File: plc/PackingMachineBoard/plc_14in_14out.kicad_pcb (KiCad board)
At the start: 2 copper layers, 208.3 x 160 mm, 241 parts, among them J1 Screw_Terminal_01x02, J10 Screw_Terminal_01x06, J11 Screw_Terminal_01x02, J12 Ethernet, J13 Screw_Terminal_01x04, J14 CAN, J15 SERIAL_1, J16 I2C0, J17 I2C1, J18 Screw_Terminal_01x01, J19 SERIAL_5, J2 Screw_Terminal_01x06, J20 Screw_Terminal_01x01, J21 Screw_Terminal_01x01, J22 Screw_Terminal_01x01, J23 Screw_Terminal_01x01, J24 Screw_Terminal_01x01, J25 Screw_Terminal_01x01, J3 Screw_Terminal_01x10, J4 Screw_Terminal_01x05, J5 Screw_Terminal_01x05, J6 RJ45_LED, J7 Screw_Terminal_01x06, J8 Screw_Terminal_01x06, J9 Screw_Terminal_01x06, K1 UMS05-1A80-75L, K2 UMS05-1A80-75L, K3 UMS05-1A80-75L, K4 UMS05-1A80-75L, K5 UMS05-1A80-75L, K6 UMS05-1A80-75L, K7 UMS05-1A80-75L, K8 UMS05-1A80-75L, Q1 IRG4PF50W, Q2 IRG4PF50W, Q3 IRG4PF50W, Q4 IRG4PF50W, Q5 IRG4PF50W, Q6 IRG4PF50W, Q7 IRG4PF50W, SW1 SW_DIP_x01, SW2 SW_DIP_x01, SW3 SW_DIP_x01, SW4 Prog, SW5 SW_DIP_x01, SW6 SW_DIP_x01, U1 tlp127, U10 TLP127, U11 tlp127, U12 tlp127, U13 tlp127, U14 tlp127, U15 74HC14, U16 74HC14, U17 74HC14, U18 74HC245, U19 Teensy3.5_All_Pins, U2 tlp127, U20 74HC245, U21 ULN2803A, U22 74AHCT125, U23 74AHCT125, U24 ENC28J60x-SS, U25 LD1117S33TR_SOT223, U26 74AHCT125, U27 74AHCT125, U28 TLP127, U29 TLP127, U3 tlp127, U30 TLP127, U31 TLP127, U32 TLP127, U33 TLP127, U34 tlp127, U35 TLP127, U36 LM7810_TO220, U4 tlp127, U5 tlp127, U6 tlp127, U7 tlp127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

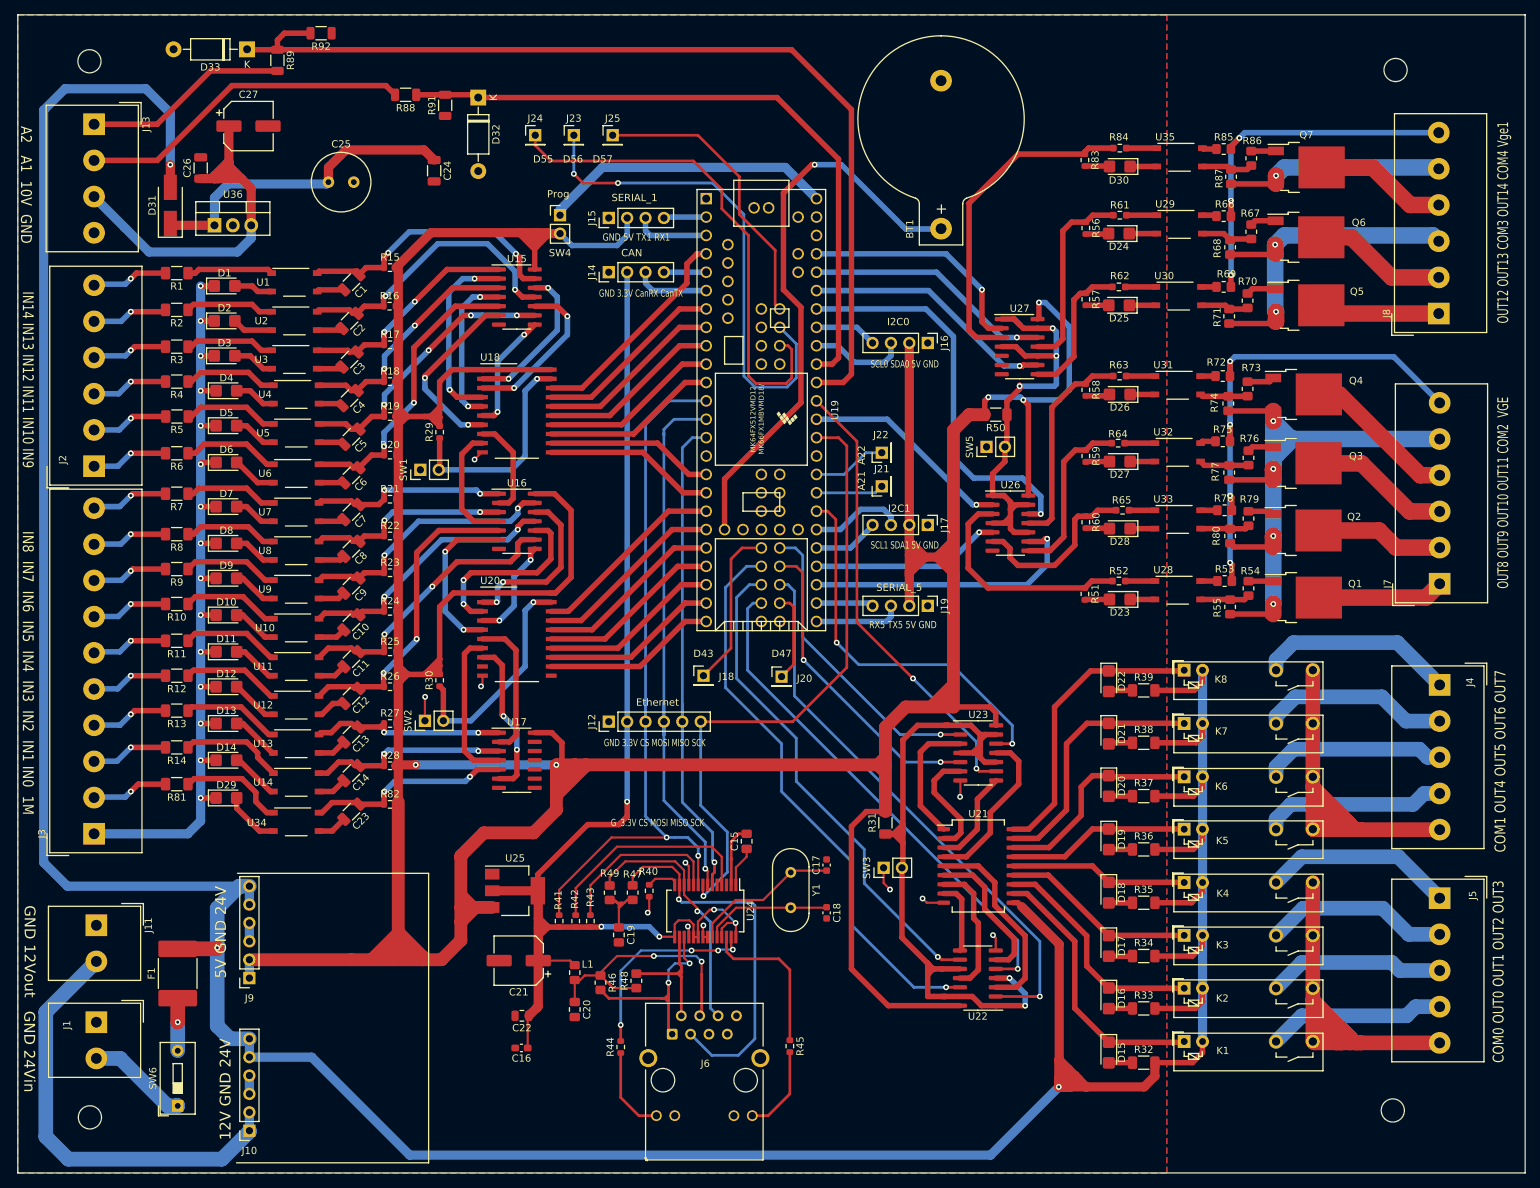
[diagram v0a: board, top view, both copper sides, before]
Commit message: Added a 3.3V and 5V pins Also commented the regulator used, and how to wire VGE and VGE1
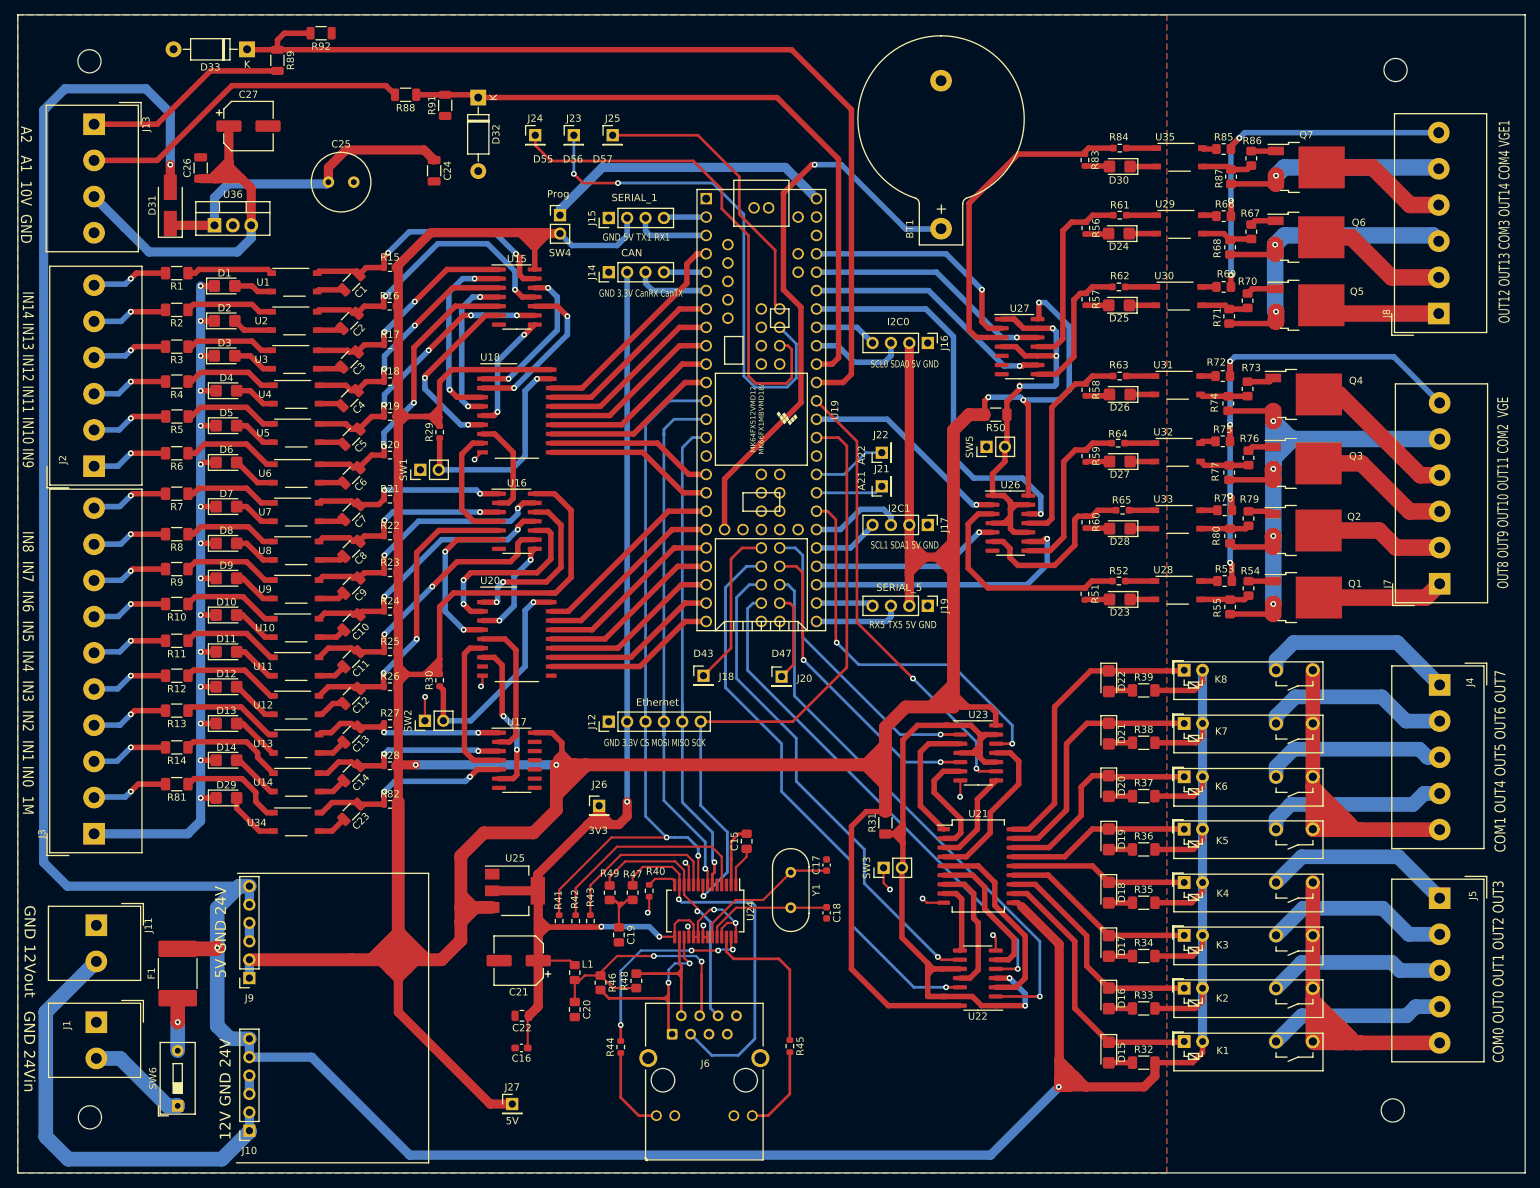
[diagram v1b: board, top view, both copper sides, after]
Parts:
- added J26: 3V3, Connector_PinHeader_2.54mm:PinHeader_1x01_P2.54mm_Vertical, F.Cu at (98.1, 122.0)
- added J27: 5V, Connector_PinHeader_2.54mm:PinHeader_1x01_P2.54mm_Vertical, F.Cu at (86.1, 163.2)
- J10: value Screw_Terminal_01x06 -> DD2712SA - 12V
- J9: value Screw_Terminal_01x06 -> DD2712SA - 5V
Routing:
- net 5V: track 816.4 -> 876.3 mm
- net 3.3V: track 172.7 -> 182.0 mm
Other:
- board text added: "OUT12 OUT13 COM3 OUT14 COM4 VGE1"
- board text removed: "G 3.3V CS MOSI MISO SCK"
- board text removed: "OUT12 OUT13 COM3 OUT14 COM4 Vge1"
